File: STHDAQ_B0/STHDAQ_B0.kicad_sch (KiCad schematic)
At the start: 5 parts, among them U1 ADS1256IDBR, U2 ADP151AUJZ-3.0-R7, U3 OPA350UA, U4 REF5025AIDR, Y1 ABLS-8.000MHZ-K4T

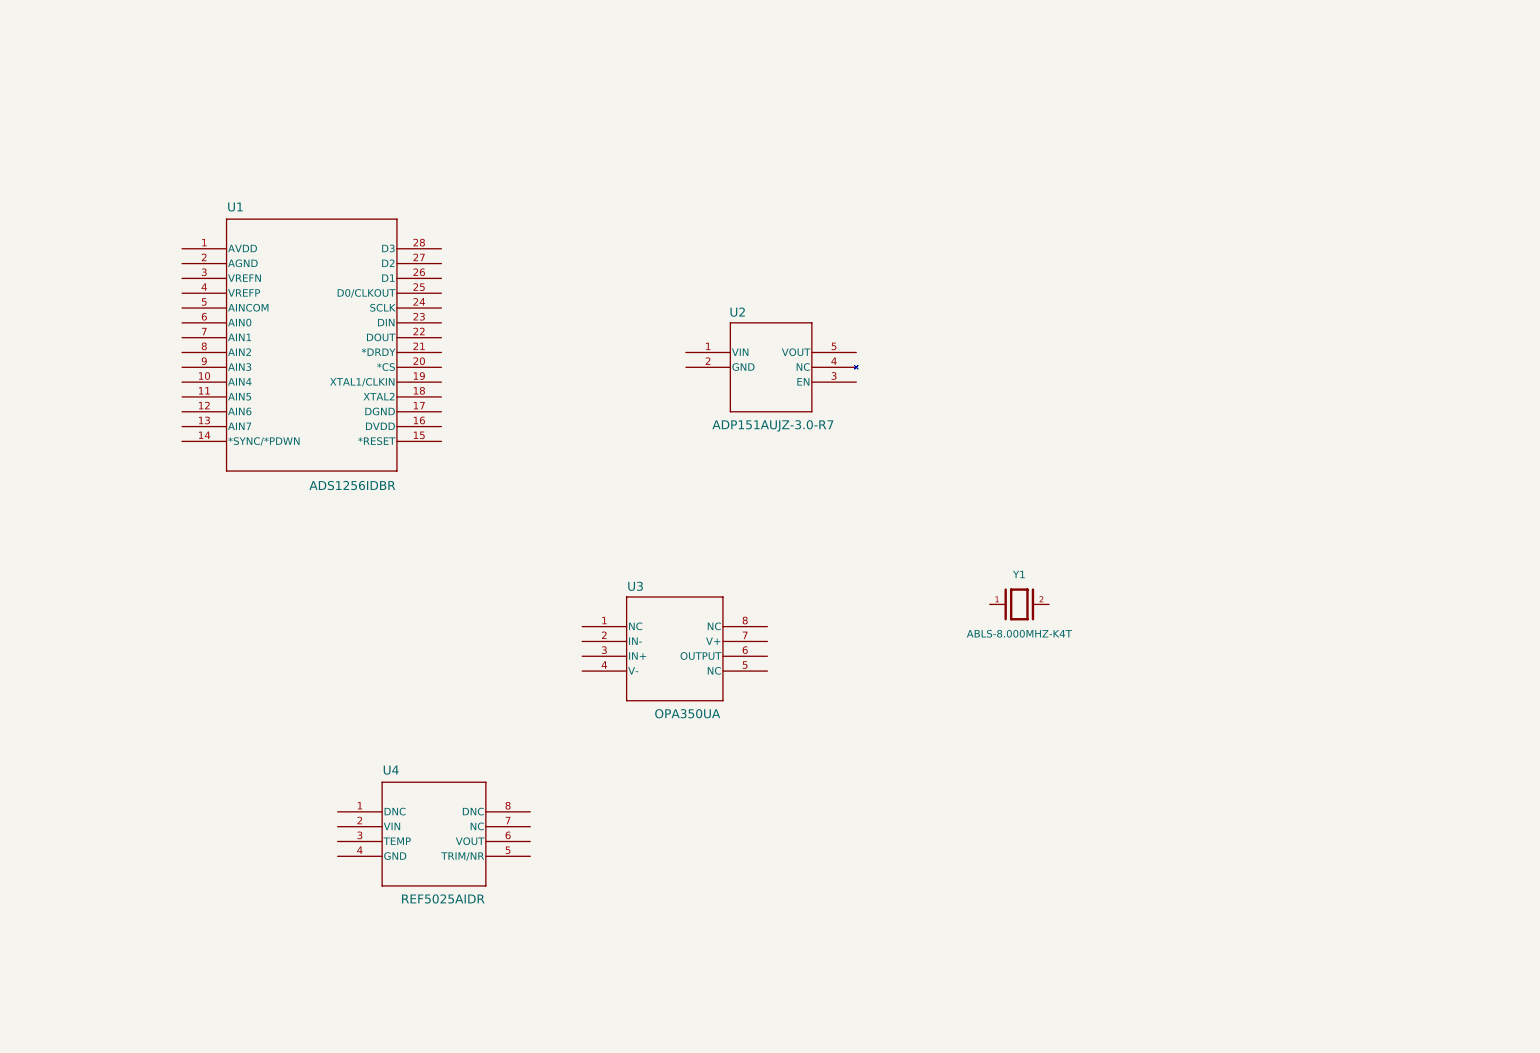
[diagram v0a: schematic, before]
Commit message: BO schematic partially (~70%) completed
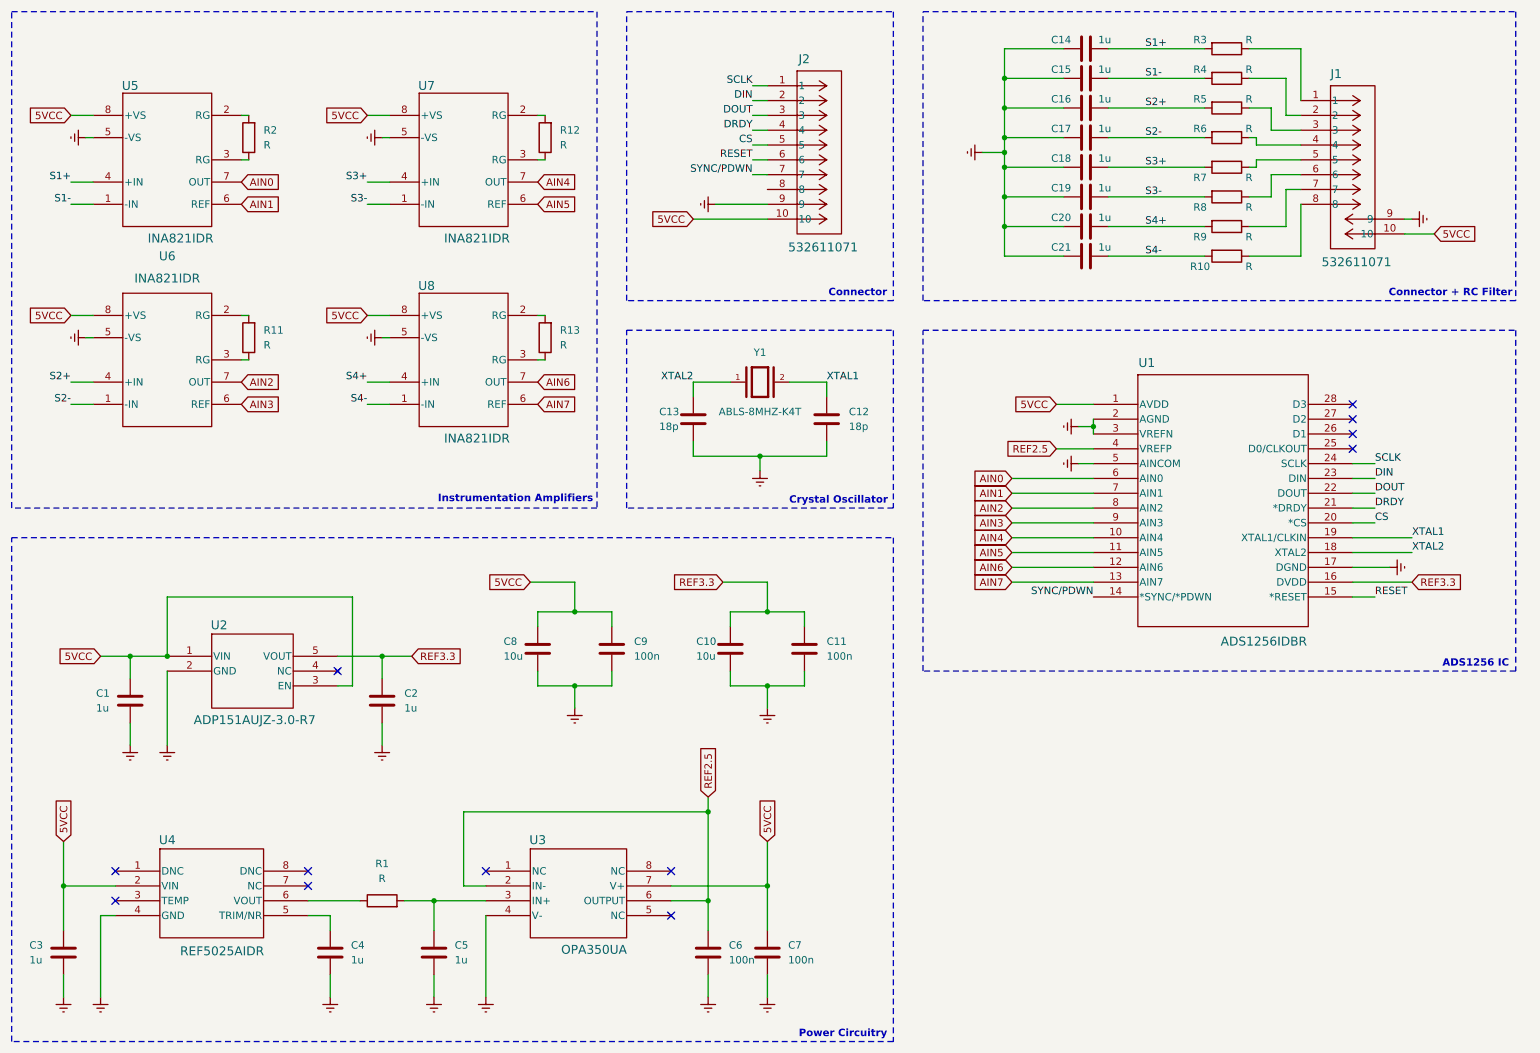
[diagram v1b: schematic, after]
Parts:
- added C1, C14, C15, C16, C17, C18, C19, C2, C20, C21, C3, C4, C5: 1u, symbol Device:C
- added C10, C8: 10u, symbol Device:C
- added C11, C6, C7, C9: 100n, symbol Device:C
- added C12, C13: 18p, symbol Device:C
- added J1: 532611071, daFootprints:CONN_532610001, symbol CONN_532610001:532611071
- added J2: 532611071, CONN_532610001-SD_10_MOL, symbol CONN_532610001:532611071
- added R1, R10, R11, R12, R13, R2, R3, R4, R5, R6, R7, R8, R9: R, symbol Device:R
- added U5, U6, U7, U8: INA821IDR, D0008A_N, symbol INA821IDR:INA821IDR
- Y1: value ABLS-8.000MHZ-K4T -> ABLS-8MHZ-K4T
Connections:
- net XTAL2: now reaches Y1.1
- net XTAL2: now also U1.18 (XTAL2), C13.2
- net XTAL1: now reaches Y1.2
- net XTAL1: now also U1.19 (XTAL1/CLKIN), C12.2
- net 5VCC: now reaches U2.1 (VIN)
- net 5VCC: now also U1.1 (AVDD), U2.3 (EN), U3.7 (V+), U4.2 (VIN), C1.2, C3.2, C7.2, C8.2, C9.2, J1.10, J2.10, U5.8 (+VS), U6.8 (+VS), U7.8 (+VS), U8.8 (+VS)
- net Earth: now reaches U2.2 (GND)
- net Earth: now also U1.17 (DGND), U1.2 (AGND), U1.3 (VREFN), U1.5 (AINCOM), U3.4 (V-), U4.4 (GND), C1.1, C10.1, C11.1, C12.1, C13.1, C14.2, C15.2, C16.2, C17.2, C18.2, C19.2, C2.1, C20.2, C21.2, C3.1, C4.1, C5.1, C6.1, C7.1, C8.1, C9.1, J1.9, J2.9, U5.5 (-VS), U6.5 (-VS), U7.5 (-VS), U8.5 (-VS)
- net REF3.3: now reaches U2.5 (VOUT)
- net REF3.3: now also U1.16 (DVDD), C10.2, C11.2, C2.2
- net at U4.5 (TRIM/NR): now also C4.2
- net at U4.6 (VOUT): now also R1.1
- net AIN4: now reaches U1.10 (AIN4)
- net AIN4: now also U7.7 (OUT)
- net AIN5: now reaches U1.11 (AIN5)
- net AIN5: now also U7.6 (REF)
- net AIN6: now reaches U1.12 (AIN6)
- net AIN6: now also U8.7 (OUT)
- net AIN7: now reaches U1.13 (AIN7)
- net AIN7: now also U8.6 (REF)
- net SYNC/PDWN: now reaches U1.14 (*SYNC/*PDWN)
- net SYNC/PDWN: now also J2.7
- net RESET: now reaches U1.15 (*RESET)
- net RESET: now also J2.6
- net CS: now reaches U1.20 (*CS)
- net CS: now also J2.5
- net DRDY: now reaches U1.21 (*DRDY)
- net DRDY: now also J2.4
- net DOUT: now reaches U1.22 (DOUT)
- net DOUT: now also J2.3
- net DIN: now reaches U1.23 (DIN)
- net DIN: now also J2.2
- net SCLK: now reaches U1.24 (SCLK)
- net SCLK: now also J2.1
- net REF2.5: now reaches U1.4 (VREFP)
- net REF2.5: now also U3.2 (IN-), U3.6 (OUTPUT), C6.2
- net AIN0: now reaches U1.6 (AIN0)
- net AIN0: now also U5.7 (OUT)
- net AIN1: now reaches U1.7 (AIN1)
- net AIN1: now also U5.6 (REF)
- net AIN2: now reaches U1.8 (AIN2)
- net AIN2: now also U6.7 (OUT)
- net AIN3: now reaches U1.9 (AIN3)
- net AIN3: now also U6.6 (REF)
- net at U3.3 (IN+): now also C5.2, R1.2
- new net: J1.1, R3.1
- new net: J1.2, R4.1
- new net: J1.3, R5.1
- new net: J1.4, R6.1
- new net: J1.5, R7.1
- new net: J1.6, R8.1
- new net: J1.7, R9.1
- new net: J1.8, R10.1
- new net: R11.2, U6.2 (RG)
- new net: R11.1, U6.3 (RG)
- new net: R13.1, U8.3 (RG)
- new net: R13.2, U8.2 (RG)
- new net: R2.1, U5.3 (RG)
- new net: R2.2, U5.2 (RG)
- new net: R12.2, U7.2 (RG)
- new net: R12.1, U7.3 (RG)
- new net S1+: C14.1, R3.2, U5.4 (+IN)
- new net S1-: C15.1, R4.2, U5.1 (-IN)
- new net S2+: C16.1, R5.2, U6.4 (+IN)
- new net S2-: C17.1, R6.2, U6.1 (-IN)
- new net S3+: C18.1, R7.2, U7.4 (+IN)
- new net S3-: C19.1, R8.2, U7.1 (-IN)
- new net S4+: C20.1, R9.2, U8.4 (+IN)
- new net S4-: C21.1, R10.2, U8.1 (-IN)
- no-connect marks 0 -> 12
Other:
- note added: "ADS1256 IC"
- note added: "Connector"
- note added: "Connector + RC Filter"
- note added: "Crystal Oscillator"
- note added: "Instrumentation Amplifiers"
- note added: "Power Circuitry"
- moved on the sheet: Y1

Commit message: started B1 schematic
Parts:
- J2: footprint CONN_532610001-SD_10_MOL -> daFootprints:CONN_532610001
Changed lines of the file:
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@@
 			)
 		)
-		(property "Footprint" "CONN_532610001-SD_10_MOL"
+		(property "Footprint" "daFootprints:CONN_532610001"
 			(at 148.59 29.21 0)
 			(effects

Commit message: prettify B1
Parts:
- U5, U6, U7, U8: footprint D0008A_N -> daFootprints:INA821IDR
- Y1: footprint ABLS-8.000MHZ-K4T:XTAL_ABLS-8.000MHZ-K4T -> daFootprints:XTAL_ABLS-8.000MHZ-K4T
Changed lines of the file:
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@@
 			)
 		)
-		(property "Footprint" "ABLS-8.000MHZ-K4T:XTAL_ABLS-8.000MHZ-K4T"
+		(property "Footprint" "daFootprints:XTAL_ABLS-8.000MHZ-K4T"
 			(at 147.32 80.01 0)
 			(effects
@@
 			)
 		)
-		(property "Footprint" "D0008A_N"
+		(property "Footprint" "daFootprints:INA821IDR"
 			(at 16.256 86.614 0)
 			(effects
@@
 			)
 		)
-		(property "Footprint" "D0008A_N"
+		(property "Footprint" "daFootprints:INA821IDR"
 			(at 67.056 86.614 0)
 			(effects
@@
 			)
 		)
-		(property "Footprint" "D0008A_N"
+		(property "Footprint" "daFootprints:INA821IDR"
 			(at 16.256 52.324 0)
 			(effects
@@
 			)
 		)
-		(property "Footprint" "D0008A_N"
+		(property "Footprint" "daFootprints:INA821IDR"
 			(at 67.056 52.324 0)
 			(effects

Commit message: added resistance values for B0
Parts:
- R1: value R -> 10k
- R10, R3, R4, R5, R6, R7, R8, R9: value R -> 1k
- R11, R12, R13, R2: value R -> 499
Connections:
- no-connect marks 12 -> 13
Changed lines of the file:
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@@
 	)
 	(no_connect
+		(at 148.59 46.99)
+	)
+	(no_connect
 		(at 132.08 171.45)
 	)
@@
 			)
 		)
-		(property "Value" "R"
+		(property "Value" "499"
 			(at 113.03 73.66 0)
 			(effects
@@
 			)
 		)
-		(property "Value" "R"
+		(property "Value" "1k"
 			(at 231.14 26.416 90)
 			(effects
@@
 			)
 		)
-		(property "Value" "R"
+		(property "Value" "1k"
 			(at 231.14 44.958 90)
 			(effects
@@
 			)
 		)
-		(property "Value" "R"
+		(property "Value" "1k"
 			(at 231.14 31.496 90)
 			(effects
@@
 			)
 		)
-		(property "Value" "R"
+		(property "Value" "499"
 			(at 62.23 39.37 0)
 			(effects
@@
 			)
 		)
-		(property "Value" "R"
+		(property "Value" "1k"
 			(at 231.14 36.576 90)
 			(effects
@@
 			)
 		)
-		(property "Value" "R"
+		(property "Value" "1k"
 			(at 231.14 50.038 90)
 			(effects
@@
 			)
 		)
-		(property "Value" "R"
+		(property "Value" "1k"
 			(at 231.14 60.198 90)
 			(effects
@@
 			)
 		)
-		(property "Value" "R"
+		(property "Value" "1k"
 			(at 231.14 21.336 90)
 			(effects
@@
 			)
 		)
-		(property "Value" "R"
+		(property "Value" "1k"
 			(at 231.14 55.118 90)
 			(effects
@@
 			)
 		)
-		(property "Value" "R"
+		(property "Value" "10k"
 			(at 82.55 165.1 90)
 			(effects
@@
 			)
 		)
-		(property "Value" "R"
+		(property "Value" "499"
 			(at 62.23 73.66 0)
 			(effects
@@
 			)
 		)
-		(property "Value" "R"
+		(property "Value" "499"
 			(at 113.03 39.37 0)
 			(effects

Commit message: B0 pcb layouting ~80% completion
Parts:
- C1, C10, C11, C12, C13, C14, C15, C16, C17, C18, C19, C2, C20, C21, C3, C4, C5, C6, C7, C8, C9: footprint (none) -> Capacitor_SMD:C_0201_0603Metric
- J1, J2: footprint daFootprints:CONN_532610001 -> Connector_Molex:Molex_CLIK-Mate_502382-1070_1x10-1MP_P1.25mm_Vertical
- R1, R10, R11, R12, R13, R2, R3, R4, R5, R6, R7, R8, R9: footprint (none) -> Resistor_SMD:R_0201_0603Metric
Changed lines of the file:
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@@
 	(wire
 		(pts
-			(xy 34.29 185.42) (xy 34.29 171.45)
-		)
-		(stroke
-			(width 0)
-			(type default)
-		)
-	)
-	(wire
-		(pts
 			(xy 231.14 48.26) (xy 234.95 48.26)
 		)
@@
 	(wire
 		(pts
+			(xy 34.29 171.45) (xy 34.29 185.42)
+		)
+		(stroke
+			(width 0)
+			(type default)
+		)
+	)
+	(wire
+		(pts
 			(xy 115.57 114.3) (xy 115.57 119.38)
 		)
@@
 			)
 		)
-		(property "Footprint" ""
+		(property "Footprint" "Capacitor_SMD:C_0201_0603Metric"
 			(at 120.9548 121.92 0)
 			(effects
@@
 			)
 		)
-		(property "Footprint" "daFootprints:CONN_532610001"
+		(property "Footprint" "Connector_Molex:Molex_CLIK-Mate_502382-1070_1x10-1MP_P1.25mm_Vertical"
 			(at 240.03 31.75 0)
 			(effects
@@
 			)
 		)
-		(property "Footprint" ""
+		(property "Footprint" "Capacitor_SMD:C_0201_0603Metric"
 			(at 199.39 23.8252 0)
 			(effects
@@
 			)
 		)
-		(property "Footprint" ""
+		(property "Footprint" "Capacitor_SMD:C_0201_0603Metric"
 			(at 134.9248 82.55 0)
 			(effects
@@
 			)
 		)
-		(property "Footprint" ""
+		(property "Footprint" "Capacitor_SMD:C_0201_0603Metric"
 			(at 199.39 54.3052 0)
 			(effects
@@
 			)
 		)
-		(property "Footprint" ""
+		(property "Footprint" "Resistor_SMD:R_0201_0603Metric"
 			(at 112.268 72.39 90)
 			(effects
@@
 			)
 		)
-		(property "Footprint" ""
+		(property "Footprint" "Capacitor_SMD:C_0201_0603Metric"
 			(at 26.9748 173.99 0)
 			(effects
@@
 			)
 		)
-		(property "Footprint" ""
+		(property "Footprint" "Resistor_SMD:R_0201_0603Metric"
 			(at 227.33 26.162 90)
 			(effects
@@
 			)
 		)
-		(property "Footprint" ""
+		(property "Footprint" "Resistor_SMD:R_0201_0603Metric"
 			(at 227.33 41.402 90)
 			(effects
@@
 			)
 		)
-		(property "Footprint" ""
+		(property "Footprint" "Capacitor_SMD:C_0201_0603Metric"
 			(at 199.39 49.2252 0)
 			(effects
@@
 			)
 		)
-		(property "Footprint" ""
+		(property "Footprint" "Resistor_SMD:R_0201_0603Metric"
 			(at 227.33 31.242 90)
 			(effects
@@
 			)
 		)
-		(property "Footprint" ""
+		(property "Footprint" "Resistor_SMD:R_0201_0603Metric"
 			(at 61.468 38.1 90)
 			(effects
@@
 			)
 		)
-		(property "Footprint" ""
+		(property "Footprint" "Resistor_SMD:R_0201_0603Metric"
 			(at 227.33 36.322 90)
 			(effects
@@
 			)
 		)
-		(property "Footprint" ""
+		(property "Footprint" "Resistor_SMD:R_0201_0603Metric"
 			(at 227.33 46.482 90)
 			(effects
@@
 			)
 		)
-		(property "Footprint" ""
+		(property "Footprint" "Resistor_SMD:R_0201_0603Metric"
 			(at 227.33 56.642 90)
 			(effects
@@
 			)
 		)
-		(property "Footprint" ""
+		(property "Footprint" "Capacitor_SMD:C_0201_0603Metric"
 			(at 72.6948 173.99 0)
 			(effects
@@
 			)
 		)
-		(property "Footprint" ""
+		(property "Footprint" "Capacitor_SMD:C_0201_0603Metric"
 			(at 38.4048 130.81 0)
 			(effects
@@
 			)
 		)
-		(property "Footprint" ""
+		(property "Footprint" "Capacitor_SMD:C_0201_0603Metric"
 			(at 90.4748 173.99 0)
 			(effects
@@
 			)
 		)
-		(property "Footprint" ""
+		(property "Footprint" "Resistor_SMD:R_0201_0603Metric"
 			(at 227.33 21.082 90)
 			(effects
@@
 			)
 		)
-		(property "Footprint" ""
+		(property "Footprint" "Capacitor_SMD:C_0201_0603Metric"
 			(at 81.5848 130.81 0)
 			(effects
@@
 			)
 		)
-		(property "Footprint" ""
+		(property "Footprint" "Capacitor_SMD:C_0201_0603Metric"
 			(at 137.4648 173.99 0)
 			(effects
@@
 			)
 		)
-		(property "Footprint" ""
+		(property "Footprint" "Capacitor_SMD:C_0201_0603Metric"
 			(at 153.9748 121.92 0)
 			(effects
@@
 			)
 		)
-		(property "Footprint" ""
+		(property "Footprint" "Capacitor_SMD:C_0201_0603Metric"
 			(at 199.39 33.9852 0)
 			(effects
@@
 			)
 		)
-		(property "Footprint" ""
+		(property "Footprint" "Capacitor_SMD:C_0201_0603Metric"
 			(at 147.6248 173.99 0)
 			(effects
@@
 			)
 		)
-		(property "Footprint" ""
+		(property "Footprint" "Resistor_SMD:R_0201_0603Metric"
 			(at 227.33 51.562 90)
 			(effects
@@
 			)
 		)
-		(property "Footprint" ""
+		(property "Footprint" "Capacitor_SMD:C_0201_0603Metric"
 			(at 199.39 28.9052 0)
 			(effects
@@
 			)
 		)
-		(property "Footprint" ""
+		(property "Footprint" "Capacitor_SMD:C_0201_0603Metric"
 			(at 141.2748 121.92 0)
 			(effects
@@
 			)
 		)
-		(property "Footprint" ""
+		(property "Footprint" "Capacitor_SMD:C_0201_0603Metric"
 			(at 199.39 44.1452 0)
 			(effects
@@
 			)
 		)
-		(property "Footprint" ""
+		(property "Footprint" "Resistor_SMD:R_0201_0603Metric"
 			(at 82.55 170.688 90)
 			(effects
@@
 			)
 		)
-		(property "Footprint" ""
+		(property "Footprint" "Capacitor_SMD:C_0201_0603Metric"
 			(at 108.2548 121.92 0)
 			(effects
@@
 			)
 		)
-		(property "Footprint" "daFootprints:CONN_532610001"
+		(property "Footprint" "Connector_Molex:Molex_CLIK-Mate_502382-1070_1x10-1MP_P1.25mm_Vertical"
 			(at 148.59 29.21 0)
 			(effects
@@
 			)
 		)
-		(property "Footprint" ""
+		(property "Footprint" "Resistor_SMD:R_0201_0603Metric"
 			(at 61.468 72.39 90)
 			(effects
@@
 			)
 		)
-		(property "Footprint" ""
+		(property "Footprint" "Capacitor_SMD:C_0201_0603Metric"
 			(at 157.7848 82.55 0)
 			(effects
@@
 			)
 		)
-		(property "Footprint" ""
+		(property "Footprint" "Resistor_SMD:R_0201_0603Metric"
 			(at 112.268 38.1 90)
 			(effects
@@
 			)
 		)
-		(property "Footprint" ""
+		(property "Footprint" "Capacitor_SMD:C_0201_0603Metric"
 			(at 199.39 59.3852 0)
 			(effects
@@
 			)
 		)
-		(property "Footprint" ""
+		(property "Footprint" "Capacitor_SMD:C_0201_0603Metric"
 			(at 199.39 39.0652 0)
 			(effects
